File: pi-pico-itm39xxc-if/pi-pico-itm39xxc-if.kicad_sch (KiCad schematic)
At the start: 29 parts, among them J1 Conn_01x03, J10 Conn_01x03, J11 Conn_02x04_Counter_Clockwise, J2 Conn_01x03, J3 Conn_01x03, J4 Conn_01x02, J5 Conn_02x05_Counter_Clockwise, J6 Conn_01x10, J7 Conn_01x02, J8 Conn_01x02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

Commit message: Working on pcb for pi pico it
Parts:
- removed J1: Conn_01x03, Connector_PinHeader_2.54mm:PinHeader_1x03_P2.54mm_Vertical, symbol Connector_Generic:Conn_01x03
- removed J11: Conn_02x04_Counter_Clockwise, Connector_PinHeader_2.54mm:PinHeader_2x04_P2.54mm_Vertical, symbol Connector_Generic:Conn_02x04_Counter_Clockwise
- removed J2: Conn_01x03, TerminalBlock_Phoenix:TerminalBlock_Phoenix_MKDS-1,5-3-5.08_1x03_P5.08mm_Horizontal, symbol Connector_Generic:Conn_01x03
- removed J5: Conn_02x05_Counter_Clockwise, Connector_PinHeader_2.54mm:PinHeader_2x05_P2.54mm_Vertical, symbol Connector_Generic:Conn_02x05_Counter_Clockwise
- removed J7: Conn_01x02, TerminalBlock_Phoenix:TerminalBlock_Phoenix_MKDS-1,5-2-5.08_1x02_P5.08mm_Horizontal, symbol Connector_Generic:Conn_01x02
- added J11: Conn_02x04_Odd_Even, Connector_PinHeader_2.54mm:PinHeader_2x04_P2.54mm_Vertical, symbol Connector_Generic:Conn_02x04_Odd_Even
- added J5: Conn_02x05_Odd_Even, Connector_PinHeader_2.54mm:PinHeader_2x05_P2.54mm_Vertical, symbol Connector_Generic:Conn_02x05_Odd_Even
- J8, J9: footprint TerminalBlock_Phoenix:TerminalBlock_Phoenix_MKDS-1,5-2-5.08_1x02_P5.08mm_Horizontal -> Connector_PinHeader_2.54mm:PinHeader_1x02_P2.54mm_Vertical
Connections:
- net PICO_GPIO26 is gone; now on net Im_ADC: U1.31 (GPIO26_ADC0)
- net +12V: now also J4.2 (Pin_2); no longer J4.1 (Pin_1)
- net +3V3: now also J9.2 (Pin_2), J11.2 (Pin_2); no longer J9.1 (Pin_1)
- net +5V: now also J8.2 (Pin_2), J5.9 (Pin_9); no longer J8.1 (Pin_1)
- net GND: now also J10.1 (Pin_1), J3.1 (Pin_1), J4.1 (Pin_1), J8.1 (Pin_1), J9.1 (Pin_1), J11.1 (Pin_1), J5.7 (Pin_7); no longer J10.3 (Pin_3), J3.3 (Pin_3), J4.2 (Pin_2), J8.2 (Pin_2), J9.2 (Pin_2)
- net Im_ADC: no longer U1.32 (GPIO27_ADC1)
- net PICO_GPIO0: now also J3.3 (Pin_3); no longer J3.1 (Pin_1)
- net PICO_GPIO14: now also J10.3 (Pin_3); no longer J10.1 (Pin_1)
- net PICO_GPIO16: now also J5.8 (Pin_8)
- net PICO_GPIO17: now also J5.4 (Pin_4)
- net PICO_GPIO18: now also J5.2 (Pin_2)
- net PICO_GPIO19: now also J5.6 (Pin_6)
- net PICO_GPIO2: now also J11.7 (Pin_7)
- net PICO_GPIO20: now also J5.5 (Pin_5)
- net PICO_GPIO21: now also J5.3 (Pin_3)
- net PICO_GPIO22: now also J11.6 (Pin_6)
- net PICO_GPIO28: now also J11.4 (Pin_4)
- net PICO_GPIO3: now also J11.5 (Pin_5)
- net PICO_GPIO8: now also J11.3 (Pin_3)
- net PICO_GPIO9: now also J11.8 (Pin_8)
- new net PICO_GPIO27: U1.32 (GPIO27_ADC1)
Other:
- sheet ttl_rs232_max3232 ports: added none; removed RX2_RS232, RX2_TTL, TX2_RS232, TX2_TTL
- note removed: "Additional RS232"
- note removed: "[5]"
- moved on the sheet: D2, D3, H1, H2, H3, H4, H5, H6, H7, J10, J3, J6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

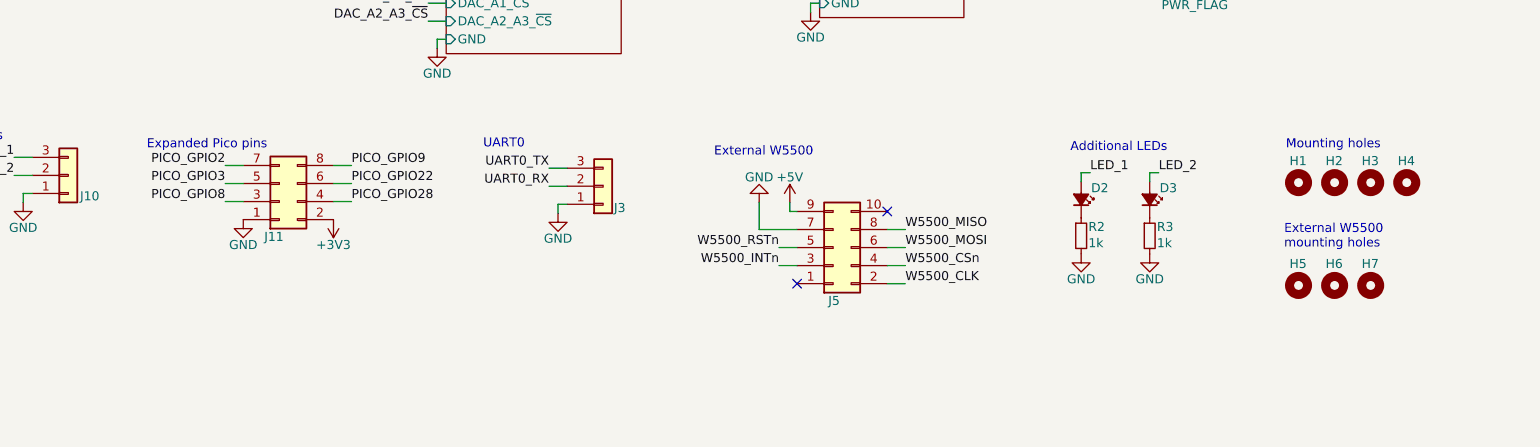
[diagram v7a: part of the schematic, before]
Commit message: Finishing pi pico itm if pcb
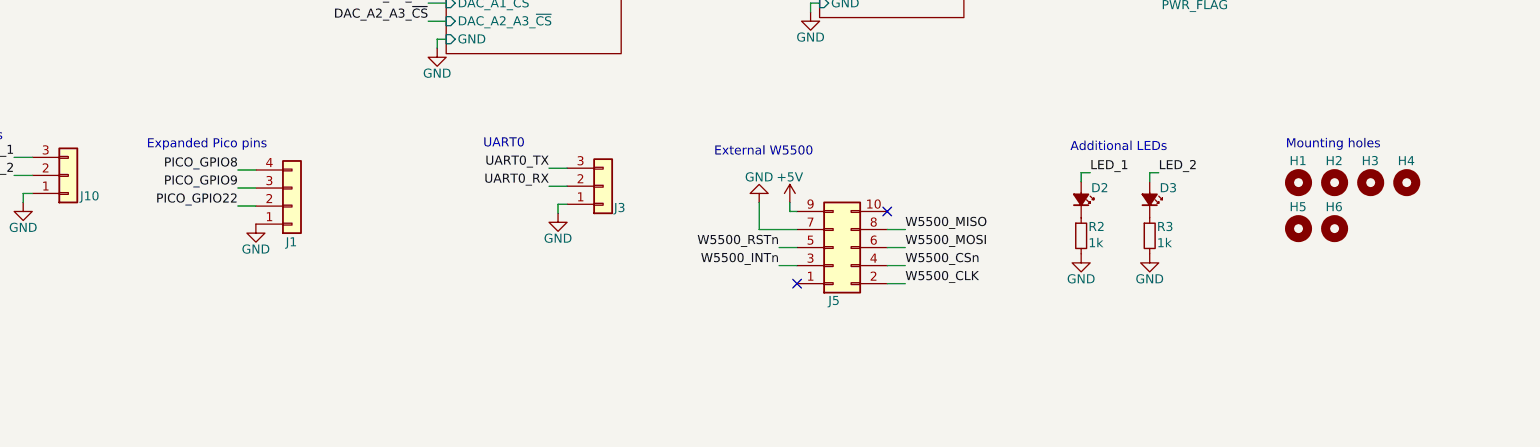
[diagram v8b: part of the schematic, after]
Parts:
- removed H7: MountingHole, MountingHole:MountingHole_3.2mm_M3, symbol Mechanical:MountingHole
- removed J11: Conn_02x04_Odd_Even, Connector_PinHeader_2.54mm:PinHeader_2x04_P2.54mm_Vertical, symbol Connector_Generic:Conn_02x04_Odd_Even
- added J1: Conn_01x04, Connector_PinHeader_2.54mm:PinHeader_1x04_P2.54mm_Vertical, symbol Connector_Generic:Conn_01x04
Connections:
- net GND: now also J1.1 (Pin_1)
- net PICO_GPIO22: now also J1.2 (Pin_2)
- net PICO_GPIO8: now also J1.4 (Pin_4)
- net PICO_GPIO9: now also J1.3 (Pin_3)
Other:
- note removed: "External W5500 mounting holes"
- moved on the sheet: H5, H6
